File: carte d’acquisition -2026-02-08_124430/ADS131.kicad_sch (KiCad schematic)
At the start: 14 parts, among them U12 ADS131M04xPW, Y3 ASCO

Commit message: Petits ajustements
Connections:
- net 3V3D renamed 3V3
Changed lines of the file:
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@@
 			)
 		)
-		(property "Value" "3V3D"
-			(at 115.57 52.07 0)
+		(property "Value" "3V3"
+			(at 118.11 55.8799 0)
 			(effects
 				(font
 					(size 1.27 1.27)
 				)
+				(justify left)
 			)
 		)

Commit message: arthur net
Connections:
- net at Y3.1 (Tri-State): now also Y3.4 (VDD)
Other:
- note added: "on fait quoi avec ?"
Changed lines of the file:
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@@
+		)
+	)
+	(text "on fait quoi avec ?"
+		(exclude_from_sim no)
+		(at 236.474 33.528 0)
+		(effects
+			(font
+				(size 1.27 1.27)
+			)
 		)
 	)
@@
 	(wire
 		(pts
+			(xy 223.52 49.53) (xy 218.44 49.53)
+		)
+		(stroke
+			(width 0)
+			(type default)
+		)
+	)
+	(wire
+		(pts
 			(xy 58.42 39.37) (xy 55.88 39.37)
 		)
@@
 	(wire
 		(pts
+			(xy 218.44 38.1) (xy 233.68 38.1)
+		)
+		(stroke
+			(width 0)
+			(type default)
+		)
+	)
+	(wire
+		(pts
 			(xy 48.26 52.07) (xy 55.88 52.07)
 		)
@@
 	(wire
 		(pts
+			(xy 233.68 38.1) (xy 233.68 41.91)
+		)
+		(stroke
+			(width 0)
+			(type default)
+		)
+	)
+	(wire
+		(pts
 			(xy 76.2 92.71) (xy 76.2 120.65)
 		)
@@
 		)
 		(stroke
+			(width 0)
+			(type default)
+		)
+	)
+	(wire
+		(pts
+			(xy 218.44 49.53) (xy 218.44 38.1)
+		)
+		(stroke

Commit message: Mis a jour plusieurs circuit et ajouter beaucoup de footprint manquant
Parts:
- removed Y3: ASCO, Oscillator:Oscillator_SMD_Abracon_ASCO-4Pin_1.6x1.2mm, symbol Oscillator:ASCO
- added C62, C63: 1u, Capacitor_SMD:C_0402_1005Metric, symbol Device:C
- added C86: 220n, Capacitor_SMD:C_0603_1608Metric, symbol Device:C
- C10, C11, C9: footprint (none) -> Capacitor_SMD:C_0603_1608Metric
- C33: renamed from C?; footprint (none) -> Capacitor_SMD:C_0603_1608Metric
- R1, R17, R2, R8: footprint (none) -> Resistor_SMD:R_0603_1608Metric
- R42, R43, R44, R46: renamed from R?; footprint (none) -> Resistor_SMD:R_0603_1608Metric
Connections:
- net 3V3: now also C63.1
- net 3V3A: now also C62.2
- net GND: now also C62.1, C63.2, C86.1
- net at U12.18 (CAP): now also C86.2
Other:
- note added: "8.192MHz high res 4.096MHz low power 2.048MHz very low power (CLKIN)Va être fournis par controleur donc trouver pin a connecter qui fonctionne"
- note removed: "CLOCK"
- note removed: "on fait quoi avec ?"

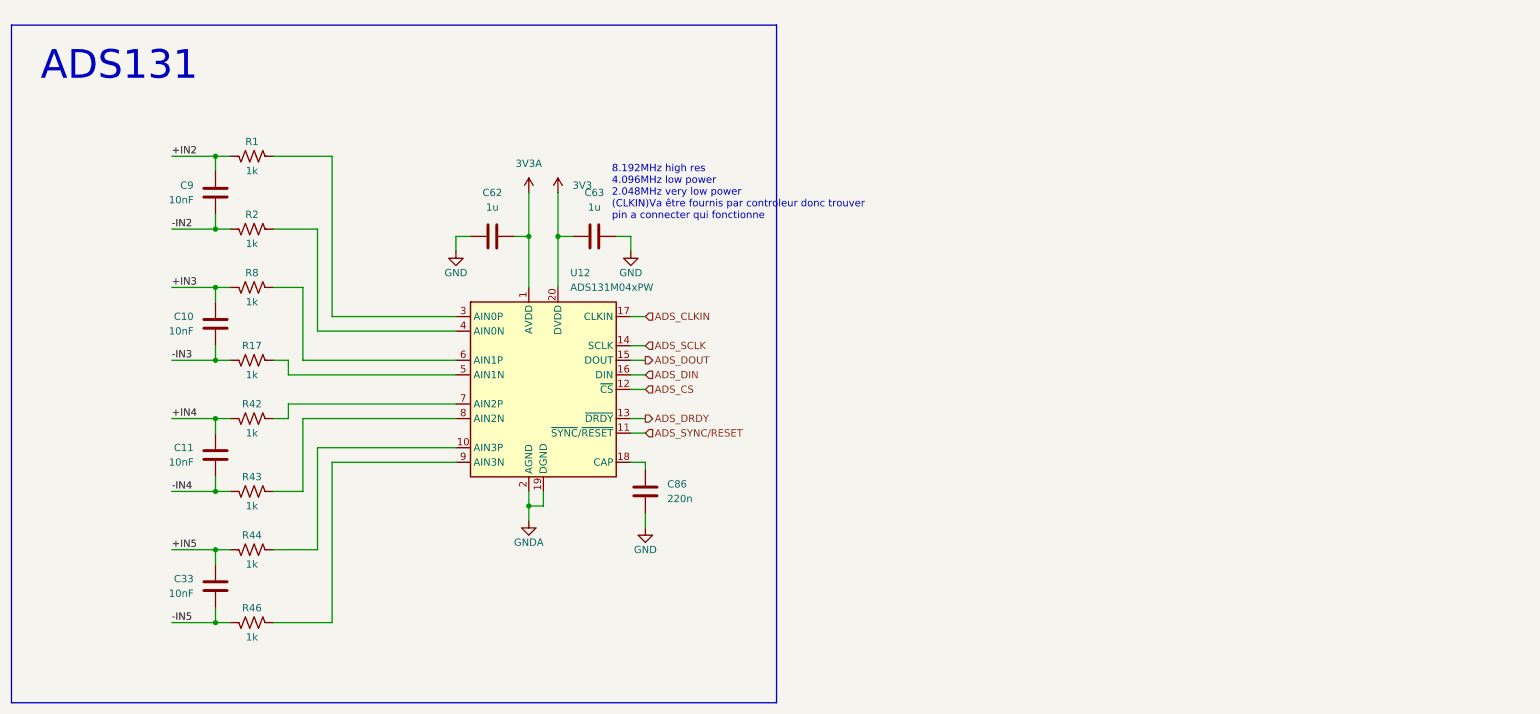
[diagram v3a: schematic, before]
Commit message: Ajout du 5VA et des borniers a vis pour loadcell
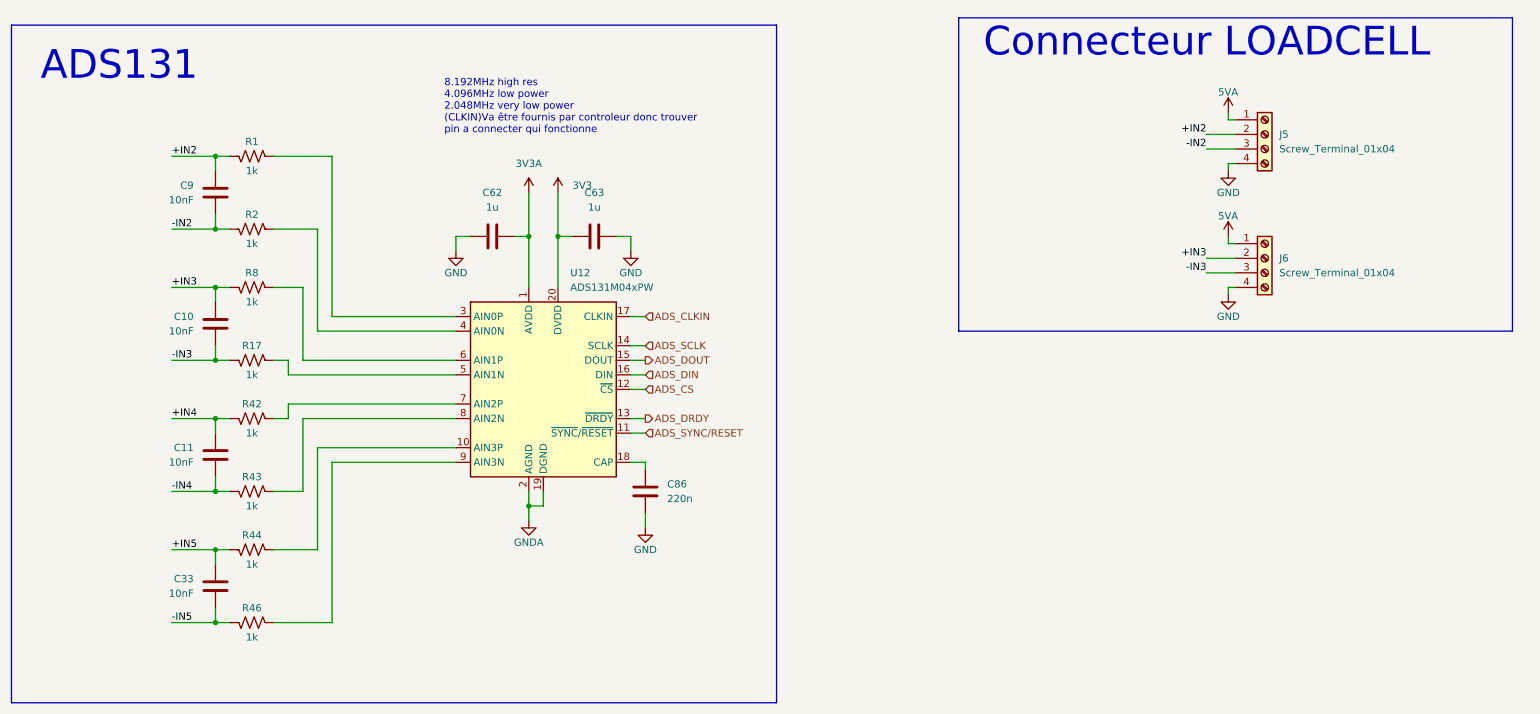
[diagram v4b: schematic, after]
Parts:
- added J5, J6: Screw_Terminal_01x04, TerminalBlock_4Ucon:TerminalBlock_4Ucon_1x04_P3.50mm_Horizontal, symbol Connector:Screw_Terminal_01x04
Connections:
- net +IN2: now also J5.2 (Pin_2)
- net +IN3: now also J6.2 (Pin_2)
- net -IN2: now also J5.3 (Pin_3)
- net -IN3: now also J6.3 (Pin_3)
- net GND: now also J5.4 (Pin_4), J6.4 (Pin_4)
- new net 5VA: J5.1 (Pin_1), J6.1 (Pin_1)
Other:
- note added: "Connecteur LOADCELL"
